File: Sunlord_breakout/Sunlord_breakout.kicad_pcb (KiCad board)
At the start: 2 copper layers, 50 x 50 mm, 11 parts, among them J1 AH, J2 AL, J3 BH, J4 BL, J5 CH, J6 CL, J7 DH, J8 DL, T1 Transformer_1P_1S

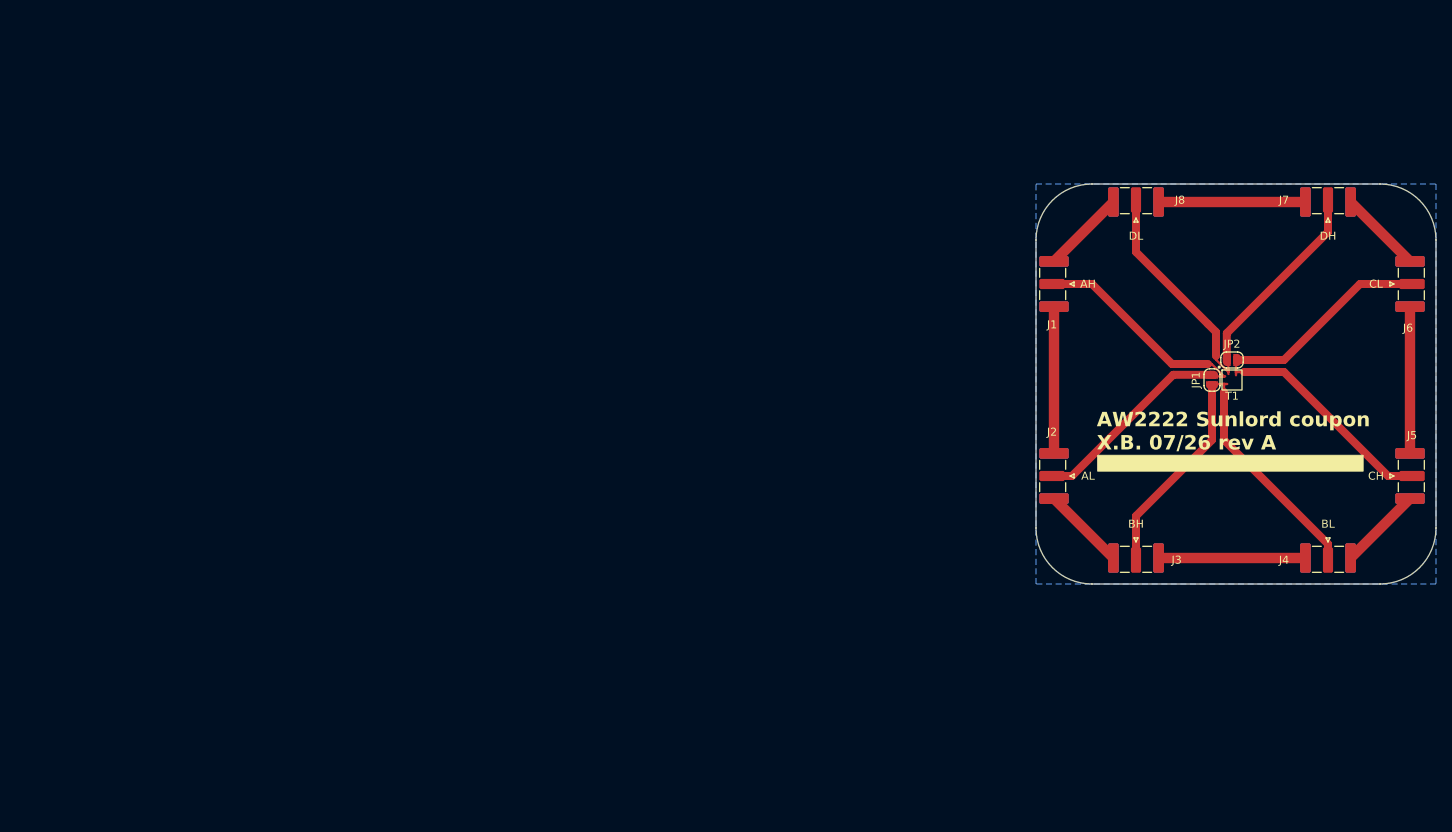
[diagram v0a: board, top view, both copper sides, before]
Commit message: added sunlord breakout
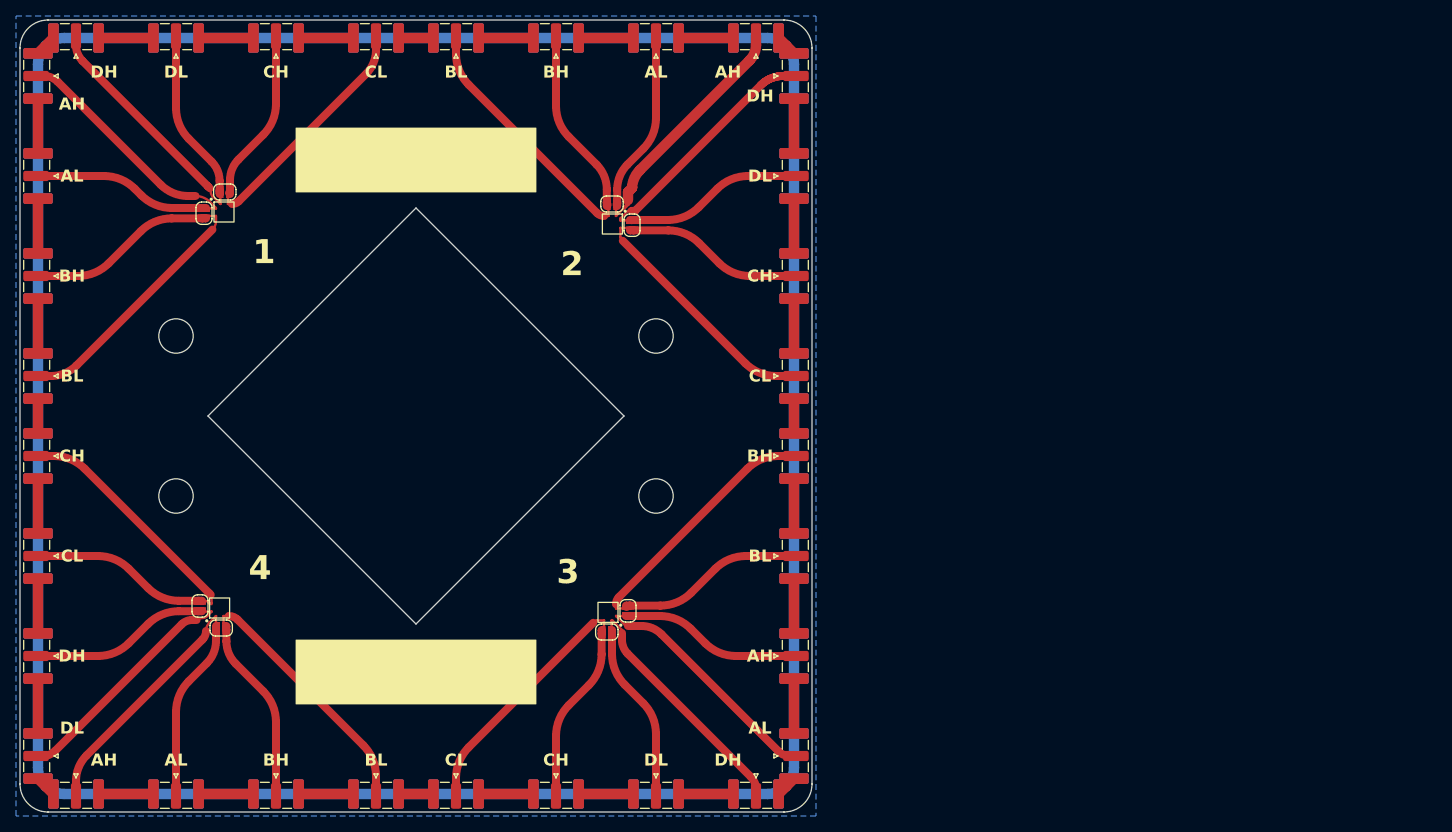
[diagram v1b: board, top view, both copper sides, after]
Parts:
- added G***: LOGO, footprints:nxp_logo, B.Cu at (74.0, 109.0)
- added J10: AL, Connector_Coaxial:SMA_Samtec_SMA-J-P-H-ST-EM1_EdgeMount, F.Cu at (104.0, 31.5)
- added J11: BH, Connector_Coaxial:SMA_Samtec_SMA-J-P-H-ST-EM1_EdgeMount, F.Cu at (91.5, 31.5)
- added J12: BL, Connector_Coaxial:SMA_Samtec_SMA-J-P-H-ST-EM1_EdgeMount, F.Cu at (79.0, 31.5)
- added J13: CH, Connector_Coaxial:SMA_Samtec_SMA-J-P-H-ST-EM1_EdgeMount, F.Cu at (121.5, 61.5)
- added J14: CL, Connector_Coaxial:SMA_Samtec_SMA-J-P-H-ST-EM1_EdgeMount, F.Cu at (121.5, 74.0)
- added J15: DH, Connector_Coaxial:SMA_Samtec_SMA-J-P-H-ST-EM1_EdgeMount, F.Cu at (121.5, 36.5)
- added J16: DL, Connector_Coaxial:SMA_Samtec_SMA-J-P-H-ST-EM1_EdgeMount, F.Cu at (121.5, 49.0)
- added J17: AH, Connector_Coaxial:SMA_Samtec_SMA-J-P-H-ST-EM1_EdgeMount, F.Cu at (121.5, 109.0)
- added J18: AL, Connector_Coaxial:SMA_Samtec_SMA-J-P-H-ST-EM1_EdgeMount, F.Cu at (121.5, 121.5)
- added J19: BH, Connector_Coaxial:SMA_Samtec_SMA-J-P-H-ST-EM1_EdgeMount, F.Cu at (121.5, 84.0)
- added J20: BL, Connector_Coaxial:SMA_Samtec_SMA-J-P-H-ST-EM1_EdgeMount, F.Cu at (121.5, 96.5)
- added J21: CH, Connector_Coaxial:SMA_Samtec_SMA-J-P-H-ST-EM1_EdgeMount, F.Cu at (91.5, 126.5)
- added J22: CL, Connector_Coaxial:SMA_Samtec_SMA-J-P-H-ST-EM1_EdgeMount, F.Cu at (79.0, 126.5)
- added J23: DH, Connector_Coaxial:SMA_Samtec_SMA-J-P-H-ST-EM1_EdgeMount, F.Cu at (116.5, 126.5)
- added J24: DL, Connector_Coaxial:SMA_Samtec_SMA-J-P-H-ST-EM1_EdgeMount, F.Cu at (104.0, 126.5)
- added J25: AH, Connector_Coaxial:SMA_Samtec_SMA-J-P-H-ST-EM1_EdgeMount, F.Cu at (31.5, 126.5)
- added J26: AL, Connector_Coaxial:SMA_Samtec_SMA-J-P-H-ST-EM1_EdgeMount, F.Cu at (44.0, 126.5)
- added J27: BH, Connector_Coaxial:SMA_Samtec_SMA-J-P-H-ST-EM1_EdgeMount, F.Cu at (56.5, 126.5)
- added J28: BL, Connector_Coaxial:SMA_Samtec_SMA-J-P-H-ST-EM1_EdgeMount, F.Cu at (69.0, 126.5)
- added J29: CH, Connector_Coaxial:SMA_Samtec_SMA-J-P-H-ST-EM1_EdgeMount, F.Cu at (26.5, 84.0)
- added J30: CL, Connector_Coaxial:SMA_Samtec_SMA-J-P-H-ST-EM1_EdgeMount, F.Cu at (26.5, 96.5)
- added J31: DH, Connector_Coaxial:SMA_Samtec_SMA-J-P-H-ST-EM1_EdgeMount, F.Cu at (26.5, 109.0)
- added J32: DL, Connector_Coaxial:SMA_Samtec_SMA-J-P-H-ST-EM1_EdgeMount, F.Cu at (26.5, 121.5)
- added J9: AH, Connector_Coaxial:SMA_Samtec_SMA-J-P-H-ST-EM1_EdgeMount, F.Cu at (116.5, 31.5)
- added JP3: A-B, Jumper:SolderJumper-2_P1.3mm_Open_RoundedPad1.0x1.5mm, F.Cu at (98.5, 52.5)
- added JP4: C-D, Jumper:SolderJumper-2_P1.3mm_Open_RoundedPad1.0x1.5mm, F.Cu at (101.0, 55.1)
- added JP5: A-B, Jumper:SolderJumper-2_P1.3mm_Open_RoundedPad1.0x1.5mm, F.Cu at (100.5, 103.3)
- added JP6: C-D, Jumper:SolderJumper-2_P1.3mm_Open_RoundedPad1.0x1.5mm, F.Cu at (97.8, 106.0)
- added JP7: A-B, Jumper:SolderJumper-2_P1.3mm_Open_RoundedPad1.0x1.5mm, F.Cu at (49.6, 105.5)
- added JP8: C-D, Jumper:SolderJumper-2_P1.3mm_Open_RoundedPad1.0x1.5mm, F.Cu at (47.0, 102.8)
- added REF**: MountingHole_4.3mm_M4, MountingHole:MountingHole_4.3mm_M4, F.Cu at (104.0, 69.0)
- added REF**: MountingHole_4.3mm_M4, MountingHole:MountingHole_4.3mm_M4, F.Cu at (44.0, 69.0)
- added REF**: MountingHole_4.3mm_M4, MountingHole:MountingHole_4.3mm_M4, F.Cu at (44.0, 89.0)
- added REF**: MountingHole_4.3mm_M4, MountingHole:MountingHole_4.3mm_M4, F.Cu at (104.0, 89.0)
- added T2: Transformer_1P_1S, footprints:AW2222_Sunlord_µXFMR, F.Cu at (99.7, 53.9)
- added T3: Transformer_1P_1S, footprints:AW2222_Sunlord_µXFMR, F.Cu at (99.1, 104.7)
- added T4: Transformer_1P_1S, footprints:AW2222_Sunlord_µXFMR, F.Cu at (48.4, 104.1)
- moved J4 163.1 mm to (26.5, 74.0), turned to 180 degrees
- moved J7 157.8 mm to (31.5, 31.5)
- moved J5 152.3 mm to (56.5, 31.5), turned to 90 degrees
- moved J3 142.0 mm to (26.5, 61.5), turned to 180 degrees
- moved J6 133.2 mm to (69.0, 31.5), turned to 90 degrees
- moved J2 132.4 mm to (26.5, 49.0)
- moved J1 129.6 mm to (26.5, 36.5)
- moved T1 127.7 mm to (48.9, 52.4)
- moved JP1 127.7 mm to (47.5, 53.6)
- moved JP2 127.6 mm to (50.1, 51.0)
- moved J8 121.7 mm to (44.0, 31.5)
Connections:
- net /A renamed /A1
- net /B renamed /B1
- net /C renamed /C1
- net /D renamed /D1
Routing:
- net /COM: track 115.4 -> 564.9 mm
- net /B4: track 0.00 -> 55.5 mm
- net /B2: track 0.00 -> 55.4 mm
- net /B3: track 0.00 -> 55.3 mm
- net /C2: track 0.00 -> 54.0 mm
- net /C3: track 0.00 -> 53.8 mm
- net /C4: track 0.00 -> 53.8 mm
- net /A2: track 0.00 -> 53.5 mm
- net /A4: track 0.00 -> 53.5 mm
- net /A3: track 0.00 -> 53.5 mm
- net /D2: track 0.00 -> 53.1 mm
- net /D3: track 0.00 -> 52.9 mm
- net /D4: track 0.00 -> 52.9 mm
- net /C1: track 55.5 -> 52.0 mm
- net /D1: track 53.7 -> 51.1 mm
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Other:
- board size 50 x 50 mm -> 99 x 99 mm
- board text added: "1"
- board text added: "2"
- board text added: "3"
- board text added: "4"
- board text added: "X.B. 08/26 revA µXFMR LCR breakout"
- board text removed: "AW2222 Sunlord coupon X.B. 07/26 rev A"
